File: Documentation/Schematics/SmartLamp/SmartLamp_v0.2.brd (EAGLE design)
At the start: 60.6 x 47 mm, 18 parts, among them IC1 DS3231/SO, U1 HM-10

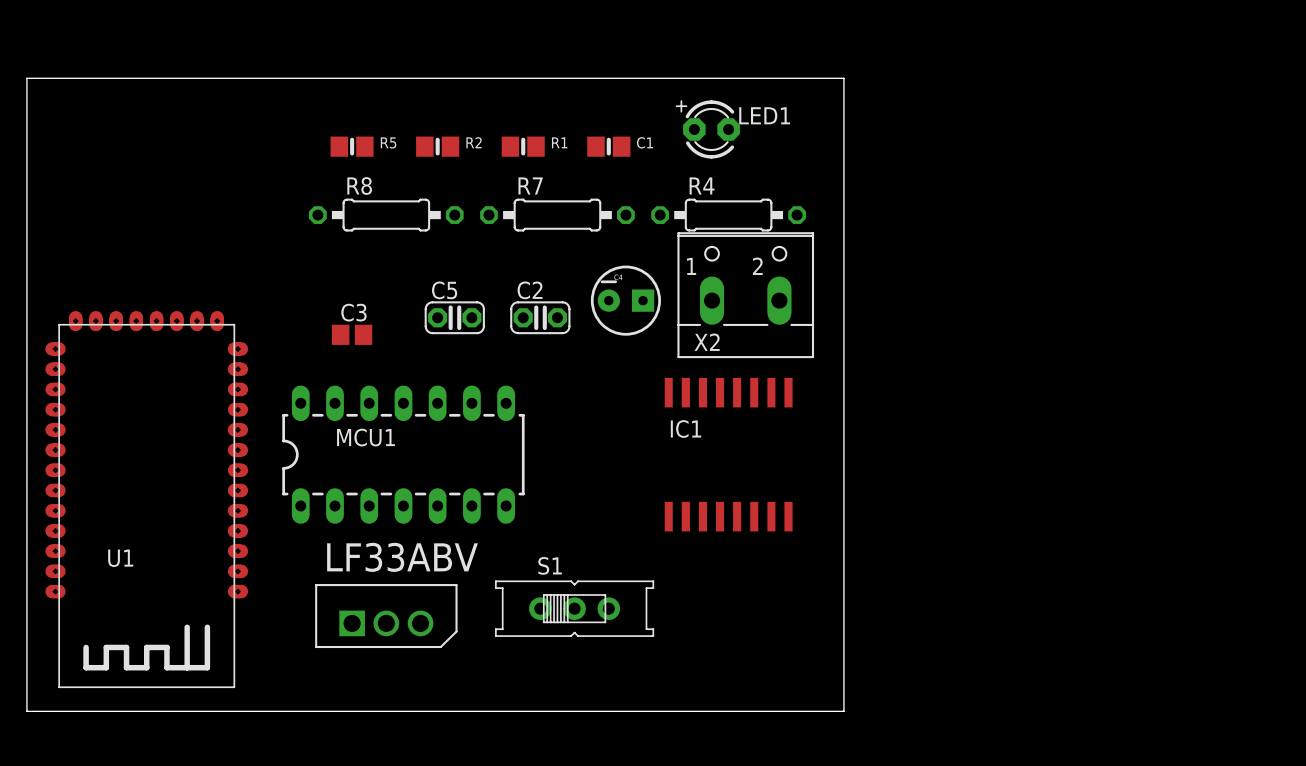
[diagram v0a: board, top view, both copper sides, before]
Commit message: Complete first version of schematic and board. Added first partlist and BOM
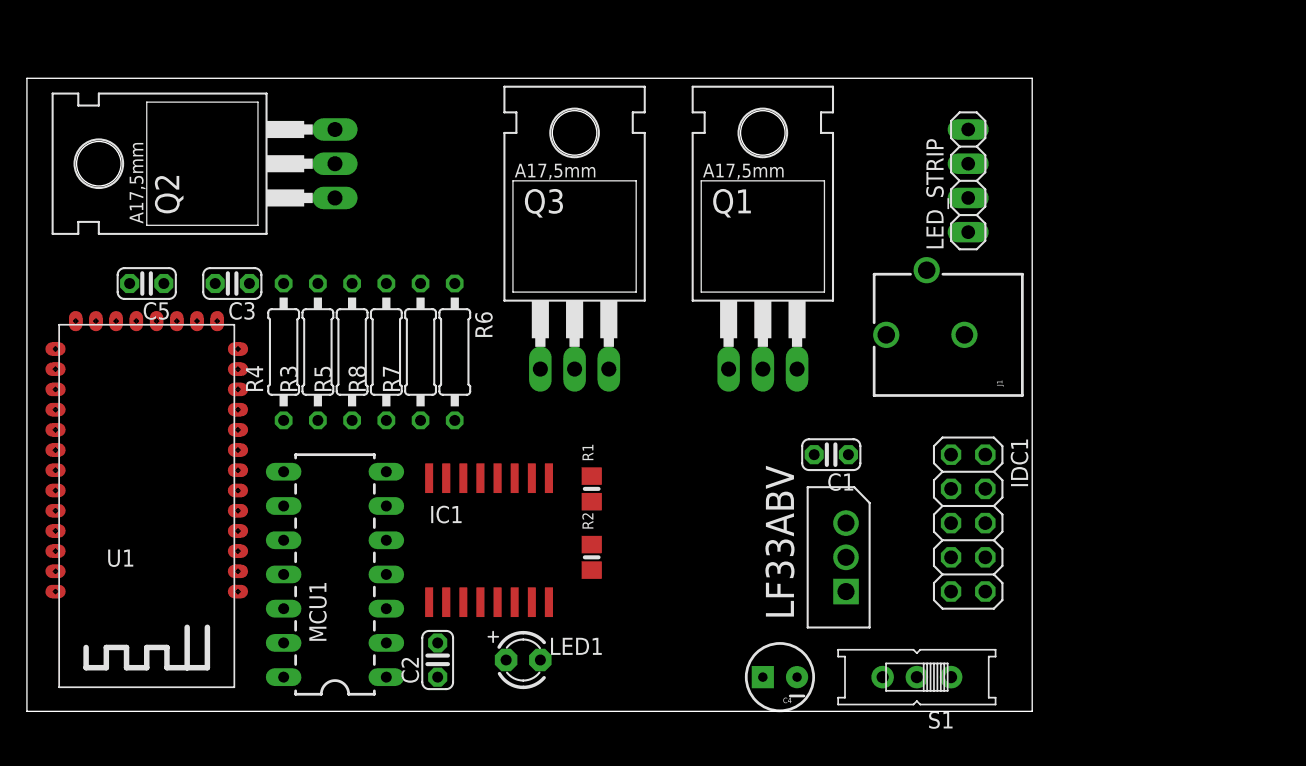
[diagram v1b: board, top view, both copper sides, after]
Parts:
- removed X2: (no value), con-wago-500:W237-102
- added IDC1: (no value), pinhead:2X05
- added J1: POWER_JACKPTH_BREAD, SparkFun-Connectors:POWER_JACK_PTH_BREAD
- added LED_STRIP: (no value), pinhead:1X04
- added Q1, Q2, Q3: IRF1404, transistor-power:TO220BH
- added R3: 240, rcl:0207/10
- added R6: 10K, rcl:0207/10
- C1: value 1uF -> 0.1uF; device microbuilder:0805-NO -> adafruit:C025-024X044
- C3: device adafruit:C0805 -> adafruit:C025-024X044
- R4: value 10K -> 240
- R5: value 10K -> 240; device microbuilder:0805-NO -> rcl:0207/10
- R7: value 470 -> 1K
- moved LED1 41.8 mm to (36.8, 3.81)
- moved R4 34.5 mm to (19.1, 26.7), turned to 90 degrees
- moved R2 32.6 mm to (41.9, 11.4), turned to 90 degrees
- moved LF33ABV 31.1 mm to (59.7, 14.0), turned to 90 degrees
- moved C4 30.2 mm to (55.9, 2.54), turned to 180 degrees
- moved C1 28.2 mm to (59.7, 19.1), turned to 180 degrees
- moved C2 26.5 mm to (30.5, 3.81), turned to 90 degrees
- moved S1 25.9 mm to (66.0, 2.54), turned to 180 degrees
- moved R1 25.9 mm to (41.9, 16.5), turned to 90 degrees
- moved C5 23.0 mm to (8.89, 31.8), turned to 180 degrees
- moved IC1 18.9 mm to (34.3, 12.7)
- moved R5 15.2 mm to (24.1, 26.7), turned to 90 degrees
- moved R7 14.4 mm to (29.2, 26.7), turned to 90 degrees
- moved R8 10.2 mm to (26.7, 26.7), turned to 90 degrees
- moved MCU1 9.92 mm to (22.9, 11.4), turned to 90 degrees
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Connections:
- removed net N$5: MCU1.4, R4.2
- removed net SQW_INT: IC1.3, R5.2
- new net !BLU_RES: MCU1.5, U1.11
- new net !INT_SQW: IC1.3, MCU1.6
- new net BLUE: IDC1.3, MCU1.9, R5.1
- new net GR: IDC1.1, MCU1.8, R4.1
- new net N$11: Q3.G, R5.2
- new net N$3: LED_STRIP.2, Q1.D
- new net N$4: LED_STRIP.3, Q2.D
- new net N$6: LED_STRIP.4, Q3.D
- new net N$7: Q1.G, R3.2
- new net N$8: Q2.G, R4.2
- new net RED: IDC1.9, MCU1.7, R3.1
- new net RESET: IDC1.5, MCU1.4, R6.2
- net +12V: now also J1.PWR, LED_STRIP.1; no longer X2.2
- net 3.3V: now also C1.1, C5.1, IDC1.10, R6.1; no longer C1.2, C5.2, R4.1, R5.1
- net GND: now also C1.2, IDC1.2, IDC1.4, J1.GND, Q1.S, Q2.S, Q3.S; no longer C1.1, X2.1
- net N$2: now also C5.2; no longer C5.1
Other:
- board size 60.6 x 47 mm -> 74.6 x 47 mm

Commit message: Added battery holder and IDC connector from Sparkfun
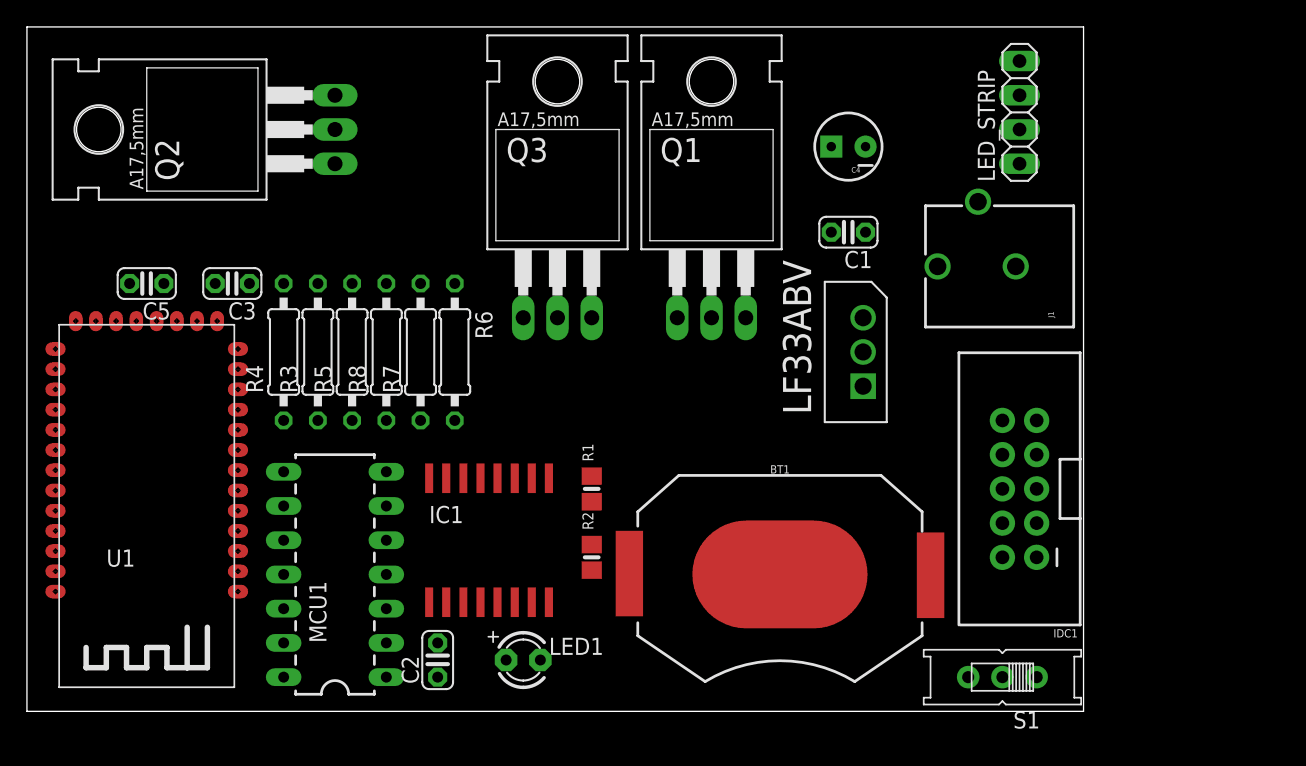
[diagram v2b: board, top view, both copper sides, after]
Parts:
- added BT1: (no value), SparkFun-Batteries:BATTCON_20MM_4LEGS
- IDC1: device pinhead:2X05 -> SparkFun-Connectors:2X5-SHROUDED
- moved C4 39.7 mm to (61.0, 41.9)
- moved C1 16.6 mm to (61.0, 35.6)
- moved LF33ABV 15.3 mm to (61.0, 29.2)
- moved LED_STRIP 6.35 mm to (73.7, 44.5)
- moved J1 6.35 mm to (81.3, 33.0)
- moved S1 6.35 mm to (72.4, 2.54)
- moved Q1 5.39 mm to (50.8, 35.6)
- moved IDC1 4.58 mm to (73.7, 16.5), turned to 180 degrees
- moved Q3 4.02 mm to (39.4, 35.6)
- moved Q2 2.54 mm to (16.5, 43.2)
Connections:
- new net N$5: BT1.NEGATIVE, IC1.14
- net GND: now also BT1.POSITIVE@1, BT1.POSITIVE@2, BT1.POSITIVE@3, BT1.POSITIVE@4; no longer IC1.14
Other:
- board size 74.6 x 47 mm -> 78.4 x 50.8 mm

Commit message: Modified switch and RGB connection
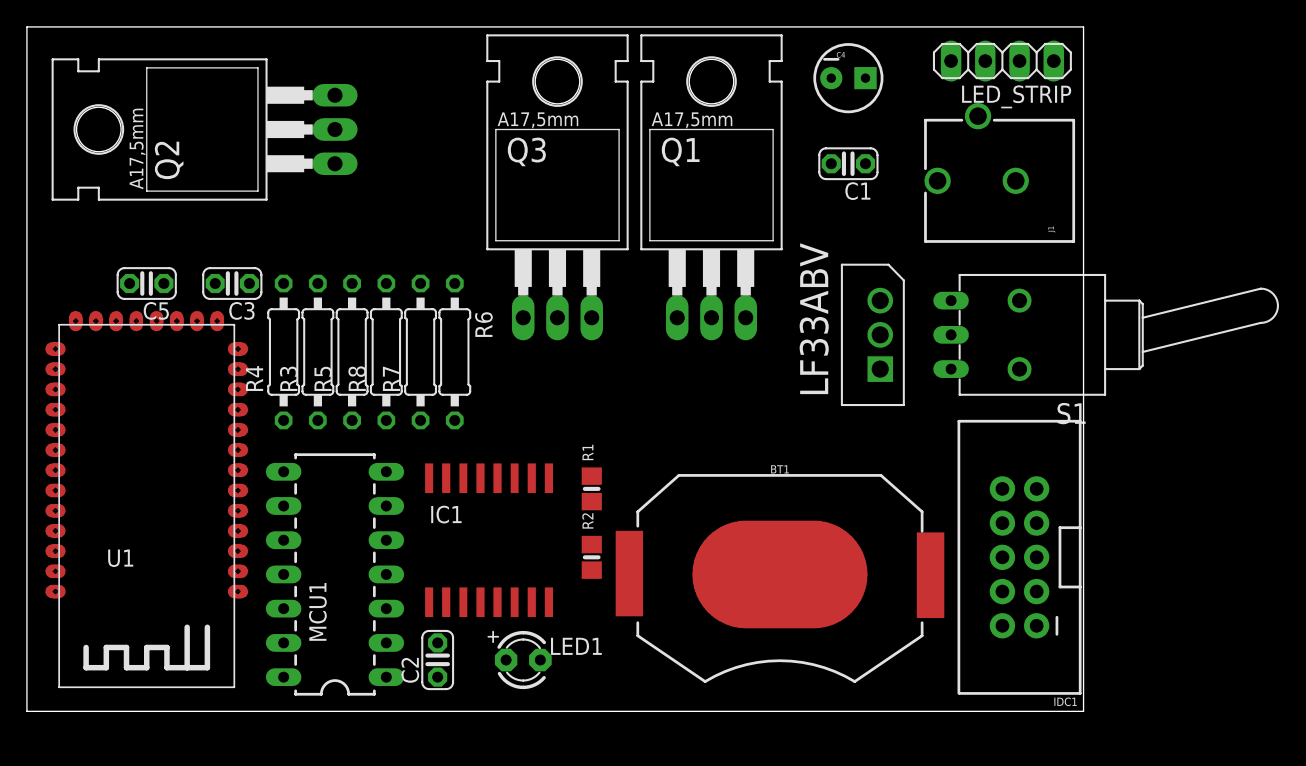
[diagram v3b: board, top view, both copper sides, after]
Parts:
- S1: device adafruit:EG1218 -> switch:9070-1W
- moved S1 25.4 mm to (73.7, 27.9)
- moved J1 6.35 mm to (81.3, 39.4)
- moved C4 5.08 mm to (61.0, 47.0), turned to 0 degrees
- moved IDC1 5.08 mm to (73.7, 11.4)
- moved C1 5.08 mm to (61.0, 40.6)
- moved LED_STRIP 4.02 mm to (72.4, 48.3), turned to 180 degrees
- moved LF33ABV 1.80 mm to (62.2, 30.5)
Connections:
- net !INT_SQW: now also MCU1.9; no longer MCU1.6
- net BLUE: now also MCU1.8; no longer MCU1.9
- net GND: no longer S1.O
- net GR: now also MCU1.7; no longer MCU1.8
- net N$1: now also S1.2, S1.B; no longer S1.P
- net N$2: now also S1.3; no longer S1.S
- net RED: now also MCU1.6; no longer MCU1.7

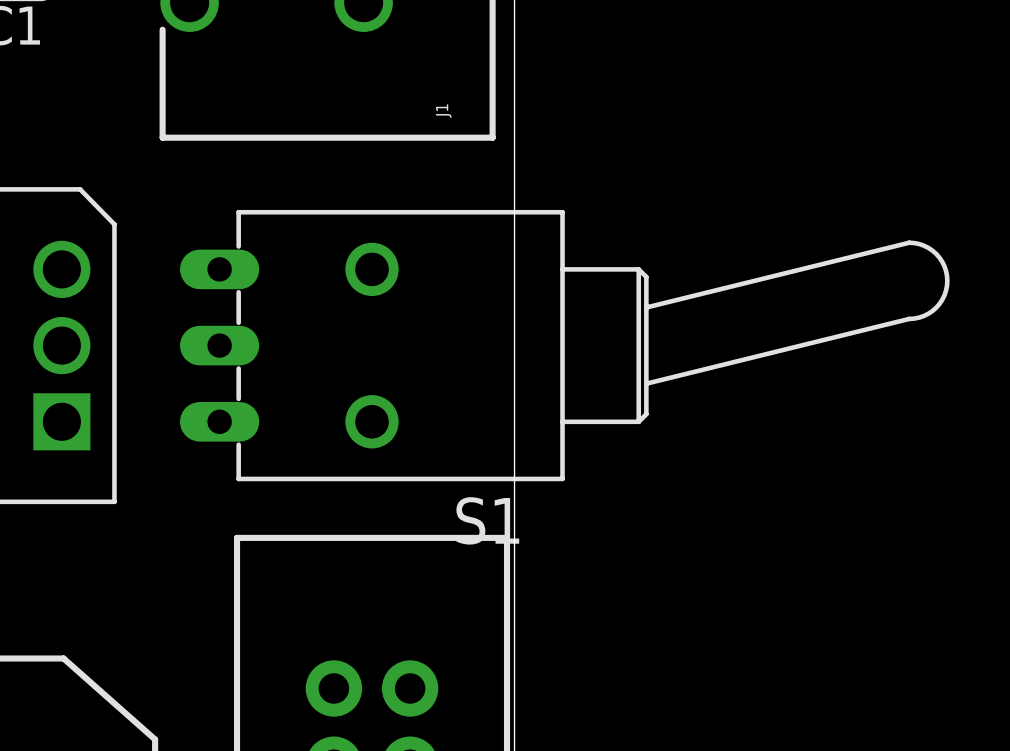
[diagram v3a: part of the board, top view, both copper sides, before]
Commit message: Fixed IDC connector and replaced switch
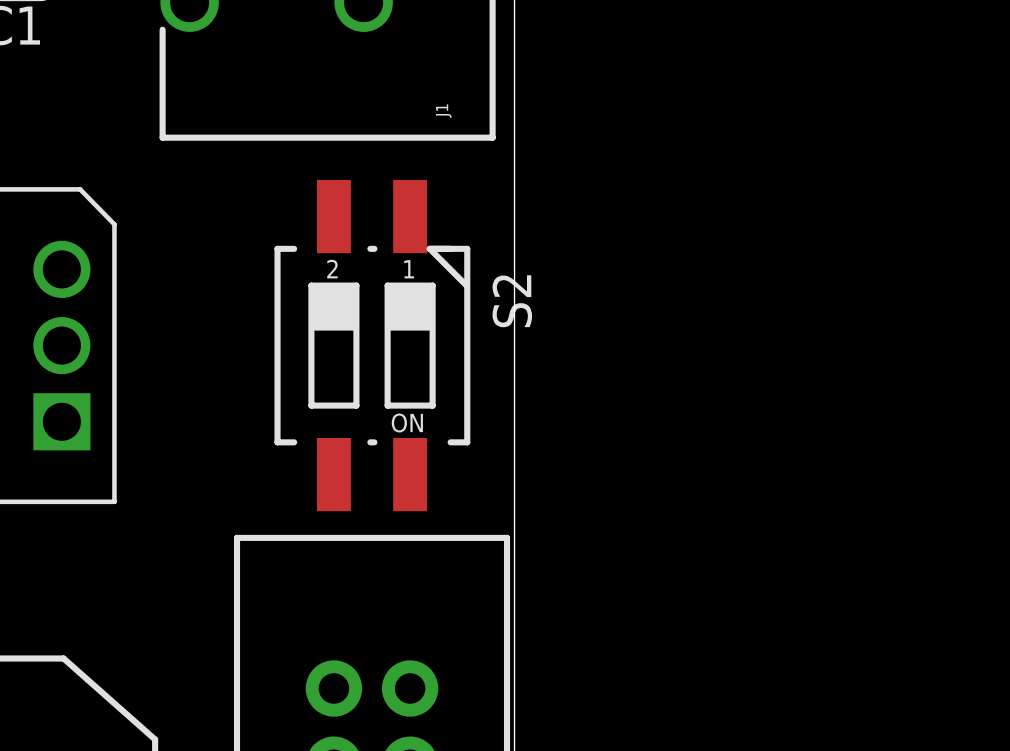
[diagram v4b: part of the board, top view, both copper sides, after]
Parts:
- removed S1: (no value), switch:9070-1W
- added S2: 219-02, switch-dil:CTS-219-02
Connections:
- new net S_OUT_DEBUG: IDC1.6, MCU1.3
- net !INT_SQW: now also IDC1.7
- net 3.3V: now also IDC1.2, S2.1; no longer C5.1, IDC1.10
- net BLUE: now also IDC1.9; no longer IDC1.3
- net GND: now also IDC1.10, IDC1.8; no longer IDC1.2, IDC1.4
- net N$1: now also C5.2; no longer S1.2, S1.B
- net N$2: now also C5.1, S2.4; no longer C5.2, S1.3
- net RED: no longer IDC1.9
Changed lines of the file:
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@@
 <element name="R8" library="rcl" package="0207/10" value="470" x="26.67" y="26.67" rot="R90"/>
 <element name="U1" library="HM-10_BLE" package="HM-10" value="HM-10" x="8.89" y="15.24" rot="R180"/>
-<element name="S1" library="switch" package="9070-1W" value="" x="73.66" y="27.94" rot="R180"/>
 <element name="Q1" library="transistor-power" package="TO220BH" value="IRF1404" x="50.8" y="35.56"/>
 <element name="Q2" library="transistor-power" package="TO220BH" value="IRF1404" x="16.51" y="43.18" rot="R90"/>
@@
 <attribute name="PROD_ID" value="BATT-10373" x="55.88" y="10.16" size="1.778" layer="27" display="off"/>
 <attribute name="SF_SKU" value="PRT-11892" x="55.88" y="10.16" size="1.778" layer="27" display="off"/>
+</element>
+<element name="S2" library="switch-dil" package="CTS-219-02" value="219-02" x="73.66" y="27.94" rot="R180">
+<attribute name="MPN" value="" x="73.66" y="27.94" size="1.778" layer="27" rot="R180" display="off"/>
+<attribute name="OC_FARNELL" value="unknown" x="73.66" y="27.94" size="1.778" layer="27" rot="R180" display="off"/>
+<attribute name="MF" value="" x="73.66" y="27.94" size="1.778" layer="27" rot="R180" display="off"/>
+<attribute name="OC_NEWARK" value="unknown" x="73.66" y="27.94" size="1.778" layer="27" rot="R180" display="off"/>
 </element>
 </elements>
@@
 <contactref element="Q2" pad="S"/>
 <contactref element="Q3" pad="S"/>
-<contactref element="IDC1" pad="4"/>
-<contactref element="IDC1" pad="2"/>
 <contactref element="J1" pad="GND"/>
 <contactref element="C1" pad="2"/>
@@
 <contactref element="BT1" pad="POSITIVE@1"/>
 <contactref element="BT1" pad="POSITIVE@2"/>
+<contactref element="IDC1" pad="8"/>
+<contactref element="IDC1" pad="10"/>
 <wire x1="59.69" y1="40.64" x2="73.38" y2="39.37" width="0" layer="19" extent="1-1"/>
 <wire x1="59.69" y1="46.99" x2="59.69" y2="40.64" width="0" layer="19" extent="1-1"/>
@@
 <wire x1="30.48" y1="5.08" x2="34.925" y2="8.1" width="0" layer="19" extent="1-1"/>
 <wire x1="19.05" y1="2.54" x2="30.48" y2="5.08" width="0" layer="19" extent="1-1"/>
-<wire x1="67.056" y1="11.684" x2="63.3222" y2="27.94" width="0" layer="19" extent="1-1"/>
+<wire x1="72.39" y1="16.51" x2="63.3222" y2="27.94" width="0" layer="19" extent="1-1"/>
+<wire x1="72.39" y1="13.97" x2="72.39" y2="16.51" width="0" layer="19" extent="1-1"/>
+<wire x1="67.056" y1="11.684" x2="72.39" y2="13.97" width="0" layer="19" extent="1-1"/>
 <wire x1="67.056" y1="8.509" x2="67.056" y2="11.684" width="0" layer="19" extent="1-1"/>
-<wire x1="72.39" y1="8.89" x2="67.056" y2="8.509" width="0" layer="19" extent="1-1"/>
-<wire x1="72.39" y1="6.35" x2="72.39" y2="8.89" width="0" layer="19" extent="1-1"/>
 <wire x1="15.66" y1="26.89" x2="33.655" y2="17.3" width="0" layer="19" extent="1-1"/>
 <wire x1="14.12" y1="28.96" x2="15.66" y2="26.89" width="0" layer="19" extent="1-1"/>
@@
 <contactref element="IC1" pad="2"/>
 <contactref element="R7" pad="1"/>
-<contactref element="C5" pad="1"/>
-<contactref element="IDC1" pad="10"/>
 <contactref element="C1" pad="1"/>
 <contactref element="C3" pad="1"/>
+<contactref element="IDC1" pad="2"/>
+<contactref element="S2" pad="1"/>
 <wire x1="62.23" y1="40.64" x2="62.23" y2="46.99" width="0" layer="19" extent="1-1"/>
 <wire x1="63.3222" y1="30.48" x2="62.23" y2="40.64" width="0" layer="19" extent="1-1"/>
-<wire x1="72.39" y1="16.51" x2="63.3222" y2="30.48" width="0" layer="19" extent="1-1"/>
+<wire x1="74.93" y1="32.24" x2="63.3222" y2="30.48" width="0" layer="19" extent="1-1"/>
+<wire x1="72.39" y1="6.35" x2="63.3222" y2="30.48" width="0" layer="19" extent="1-1"/>
 <wire x1="41.91" y1="15.56" x2="63.3222" y2="30.48" width="0" layer="19" extent="1-1"/>
 <wire x1="41.91" y1="10.48" x2="41.91" y2="15.56" width="0" layer="19" extent="1-1"/>
@@
 <wire x1="31.75" y1="31.75" x2="29.21" y2="21.59" width="0" layer="19" extent="1-1"/>
 <wire x1="16.51" y1="31.75" x2="31.75" y2="31.75" width="0" layer="19" extent="1-1"/>
-<wire x1="10.16" y1="31.75" x2="16.51" y2="31.75" width="0" layer="19" extent="1-1"/>
 </signal>
 <signal name="!INT_SQW">
 <contactref element="IC1" pad="3"/>
 <contactref element="MCU1" pad="9"/>
+<contactref element="IDC1" pad="7"/>
+<wire x1="32.385" y1="8.1" x2="74.93" y2="13.97" width="0" layer="19" extent="1-1"/>
 <wire x1="19.05" y1="15.24" x2="32.385" y2="8.1" width="0" layer="19" extent="1-1"/>
 </signal>
@@
 <wire x1="2.12" y1="25.39" x2="29.21" y2="31.75" width="0" layer="19" extent="1-1"/>
 </signal>
-<signal name="N$1">
-<contactref element="S1" pad="2"/>
-<contactref element="U1" pad="12"/>
-<contactref element="S1" pad="B"/>
-<wire x1="68.58" y1="27.94" x2="73.66" y2="30.48" width="0" layer="19" extent="1-1"/>
-<wire x1="15.66" y1="25.39" x2="68.58" y2="27.94" width="0" layer="19" extent="1-1"/>
-</signal>
-<signal name="N$2">
-<contactref element="C5" pad="2"/>
-<contactref element="S1" pad="3"/>
-<wire x1="7.62" y1="31.75" x2="68.58" y2="25.4" width="0" layer="19" extent="1-1"/>
-</signal>
 <signal name="N$3">
 <contactref element="Q1" pad="D"/>
@@
 <signal name="RED">
 <contactref element="R3" pad="1"/>
-<contactref element="IDC1" pad="9"/>
 <contactref element="MCU1" pad="6"/>
-<wire x1="26.67" y1="15.24" x2="74.93" y2="16.51" width="0" layer="19" extent="1-1"/>
-<wire x1="21.59" y1="21.59" x2="26.67" y2="15.24" width="0" layer="19" extent="1-1"/>
+<wire x1="26.67" y1="15.24" x2="21.59" y2="21.59" width="0" layer="19" extent="1-1"/>
 </signal>
 <signal name="GR">
 <contactref element="R4" pad="1"/>
+<contactref element="MCU1" pad="7"/>
 <contactref element="IDC1" pad="1"/>
-<contactref element="MCU1" pad="7"/>
 <wire x1="26.67" y1="17.78" x2="74.93" y2="6.35" width="0" layer="19" extent="1-1"/>
 <wire x1="19.05" y1="21.59" x2="26.67" y2="17.78" width="0" layer="19" extent="1-1"/>
@@
 <signal name="BLUE">
 <contactref element="R5" pad="1"/>
-<contactref element="IDC1" pad="3"/>
 <contactref element="MCU1" pad="8"/>
-<wire x1="24.13" y1="21.59" x2="74.93" y2="8.89" width="0" layer="19" extent="1-1"/>
+<contactref element="IDC1" pad="9"/>
+<wire x1="24.13" y1="21.59" x2="74.93" y2="16.51" width="0" layer="19" extent="1-1"/>
 <wire x1="19.05" y1="17.78" x2="24.13" y2="21.59" width="0" layer="19" extent="1-1"/>
 </signal>
@@
 <wire x1="32.385" y1="17.3" x2="55.88" y2="10.16" width="0" layer="19" extent="1-1"/>
 </signal>
+<signal name="S_OUT_DEBUG">
+<contactref element="MCU1" pad="3"/>
+<contactref element="IDC1" pad="6"/>
+<wire x1="26.67" y1="7.62" x2="72.39" y2="11.43" width="0" layer="19" extent="1-1"/>
+</signal>
+<signal name="N$1">
+<contactref element="U1" pad="12"/>
+<contactref element="C5" pad="2"/>
+<wire x1="7.62" y1="31.75" x2="15.66" y2="25.39" width="0" layer="19" extent="1-1"/>
+</signal>
+<signal name="N$2">
+<contactref element="S2" pad="4"/>
+<contactref element="C5" pad="1"/>
+<wire x1="10.16" y1="31.75" x2="74.93" y2="23.64" width="0" layer="19" extent="1-1"/>
+</signal>
 </signals>
